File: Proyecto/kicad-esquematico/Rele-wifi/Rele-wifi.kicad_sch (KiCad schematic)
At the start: 10 parts, among them J1 TB_1X3, J2 TB_1X3, K1 RELAY_C, Q1 BC547, U1 ESP32, U3 PC817

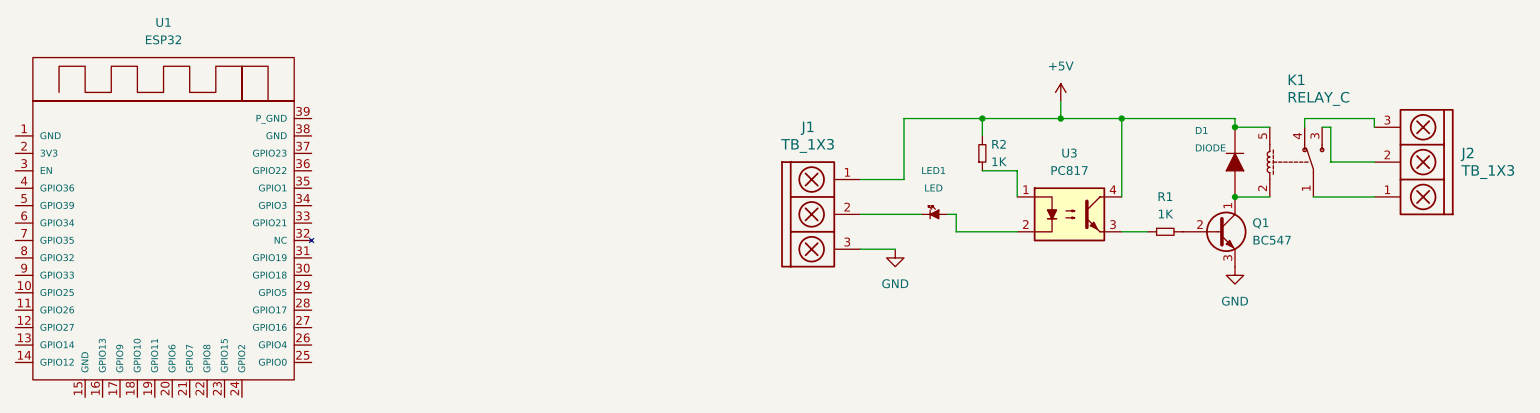
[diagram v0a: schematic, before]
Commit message: cambio en el informe, colocacion de huellas del rele y inicio del PCB
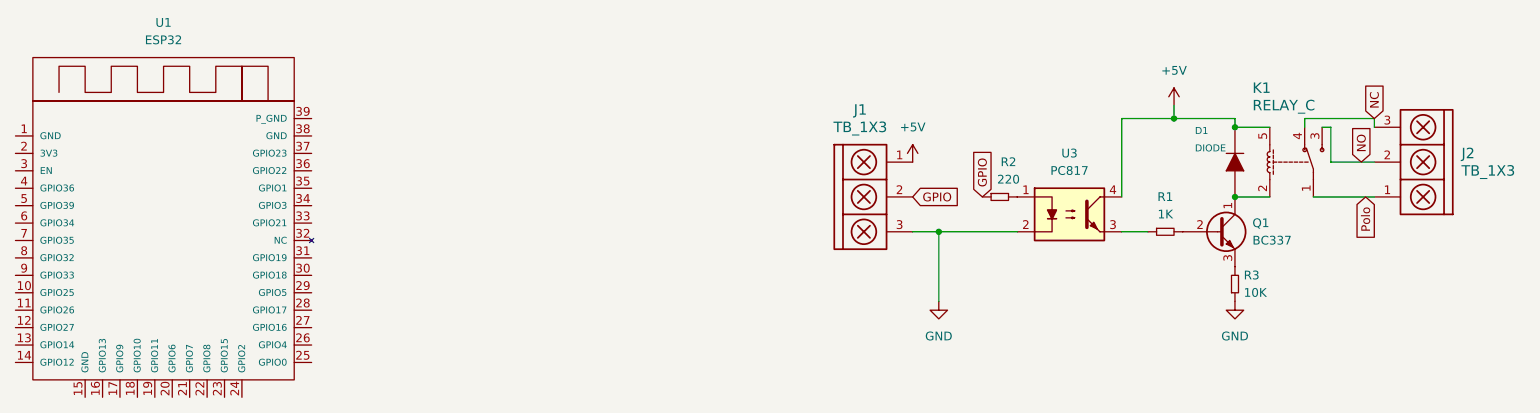
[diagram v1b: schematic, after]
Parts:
- removed LED1: LED, symbol EESTN5:LED
- added R3: 10K, Resistor_THT:R_Axial_DIN0207_L6.3mm_D2.5mm_P10.16mm_Horizontal, symbol EESTN5:R
- D1: footprint (none) -> Diode_THT:D_5W_P12.70mm_Horizontal
- J1, J2: footprint (none) -> Connector_PinHeader_2.54mm:PinHeader_1x03_P2.54mm_Vertical
- K1: footprint (none) -> Relay_THT:Relay_SPDT_SANYOU_SRD_Series_Form_C
- Q1: value BC547 -> BC337; footprint EESTN5:TO-92 -> Package_TO_SOT_THT:TO-92_Inline
- R1: footprint (none) -> Resistor_THT:R_Axial_DIN0207_L6.3mm_D2.5mm_P10.16mm_Horizontal
- R2: value 1K -> 220; footprint (none) -> Resistor_THT:R_Axial_DIN0207_L6.3mm_D2.5mm_P10.16mm_Horizontal
- U3: footprint Housings_DIP:DIP-4_W7.62mm -> Package_DIP:DIP-4_W7.62mm
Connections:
- net +5V: no longer R2.2
- net GND: now also U3.2, R3.1; no longer Q1.3 (E)
- net at U3.1: now also R2.2; no longer R2.1
- net GPIO: now reaches J1.2
- net GPIO: now also R2.1
- net Polo: now reaches J2.1, K1.1
- net NO: now reaches J2.2, K1.3
- net NC: now reaches J2.3, K1.4
- new net: Q1.3 (E), R3.2
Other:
- moved on the sheet: R2
